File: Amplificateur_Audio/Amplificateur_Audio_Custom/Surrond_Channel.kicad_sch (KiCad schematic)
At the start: 80 parts, among them J401 SL+, J402 SL-, J403 SR+, J404 SR-, J405 Analog input Connector, U401 PCM5252RHBR, U402 TPA3244DDWR, U403 74LVC1G125, U404 74LVC1G125

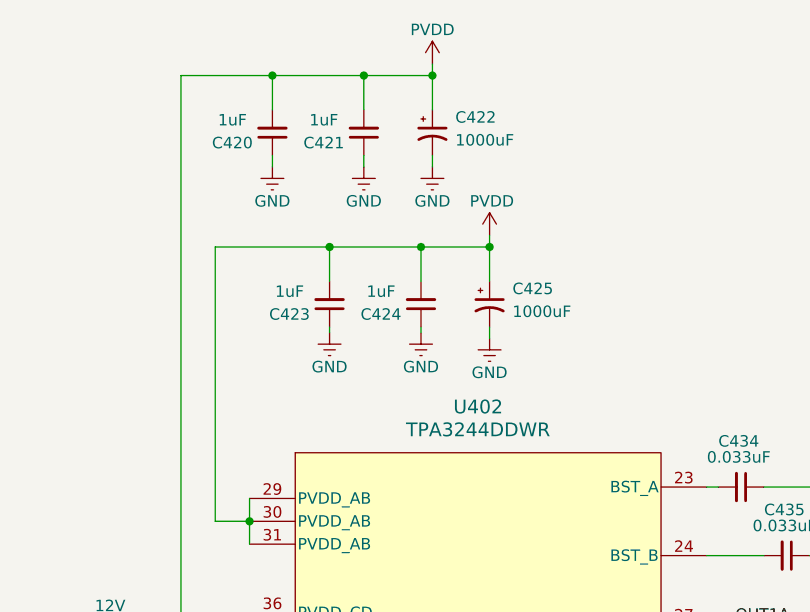
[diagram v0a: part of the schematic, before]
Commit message: Placement casi définitif prochaine étape vias de GND + stitching
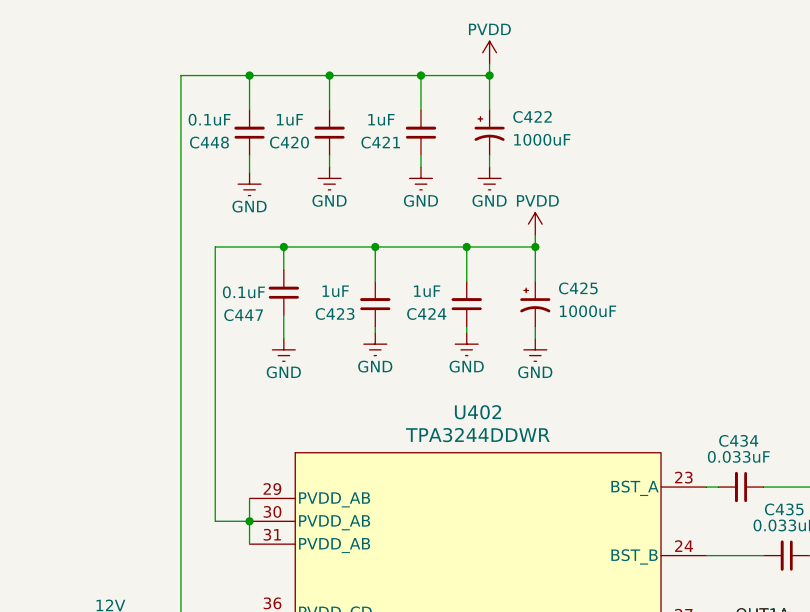
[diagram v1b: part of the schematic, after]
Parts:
- added C447, C448: 0.1uF, Capacitor_SMD:C_0603_1608Metric, symbol Device:C_Small
- C410, C411, C432, C433: footprint Capacitor_SMD:C_0402_1005Metric_Pad0.74x0.62mm_HandSolder -> Capacitor_SMD:C_0402_1005Metric
- C420, C421, C423, C424: footprint Capacitor_SMD:C_1206_3216Metric_Pad1.33x1.80mm_HandSolder -> Capacitor_SMD:C_1206_3216Metric
- C434, C435, C437, C439, C442, C443, C444, C445: footprint Capacitor_SMD:C_0603_1608Metric_Pad1.08x0.95mm_HandSolder -> Capacitor_SMD:C_0603_1608Metric
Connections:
- net GND: now also C447.1, C448.1
- net PVDD: now also C447.2, C448.2
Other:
- moved on the sheet: C420, C421, C422, C423, C424, C425

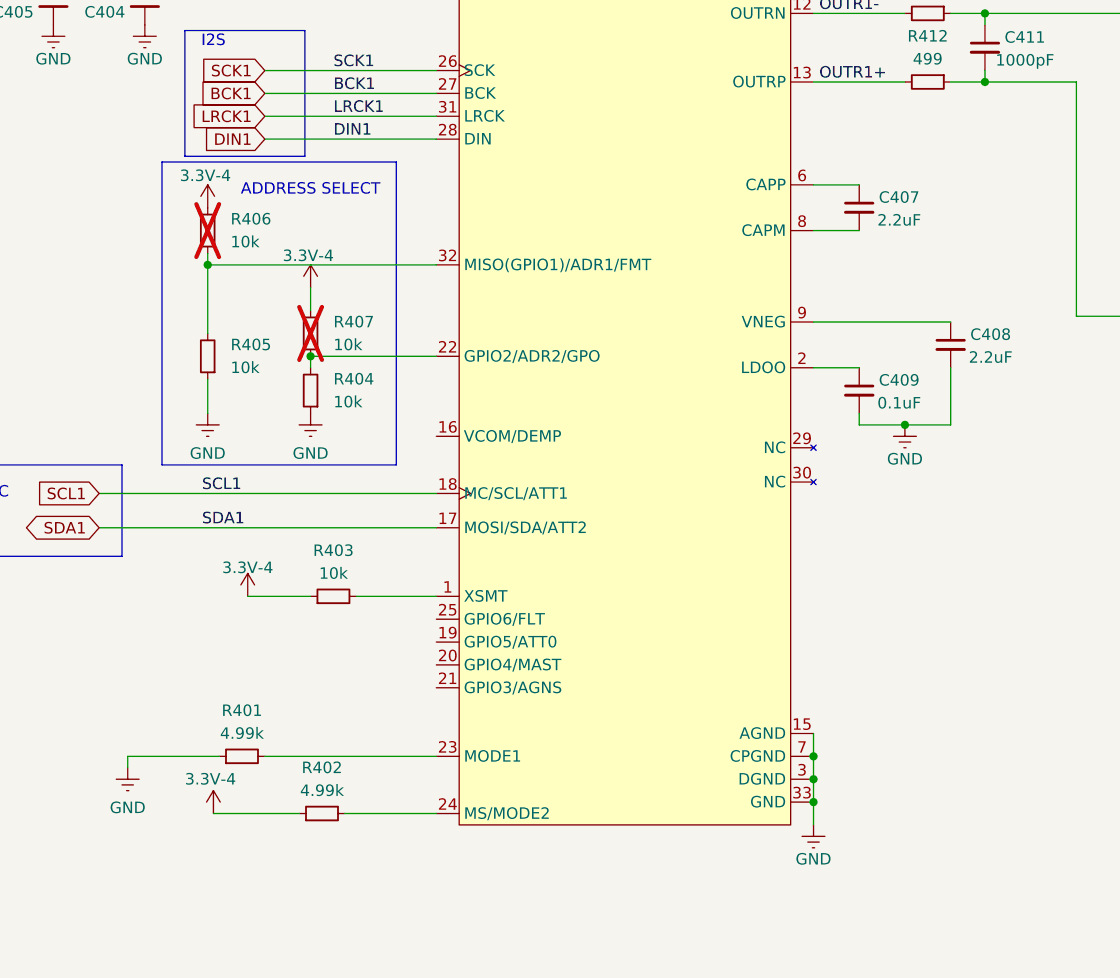
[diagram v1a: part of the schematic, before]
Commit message: Affinage du routage
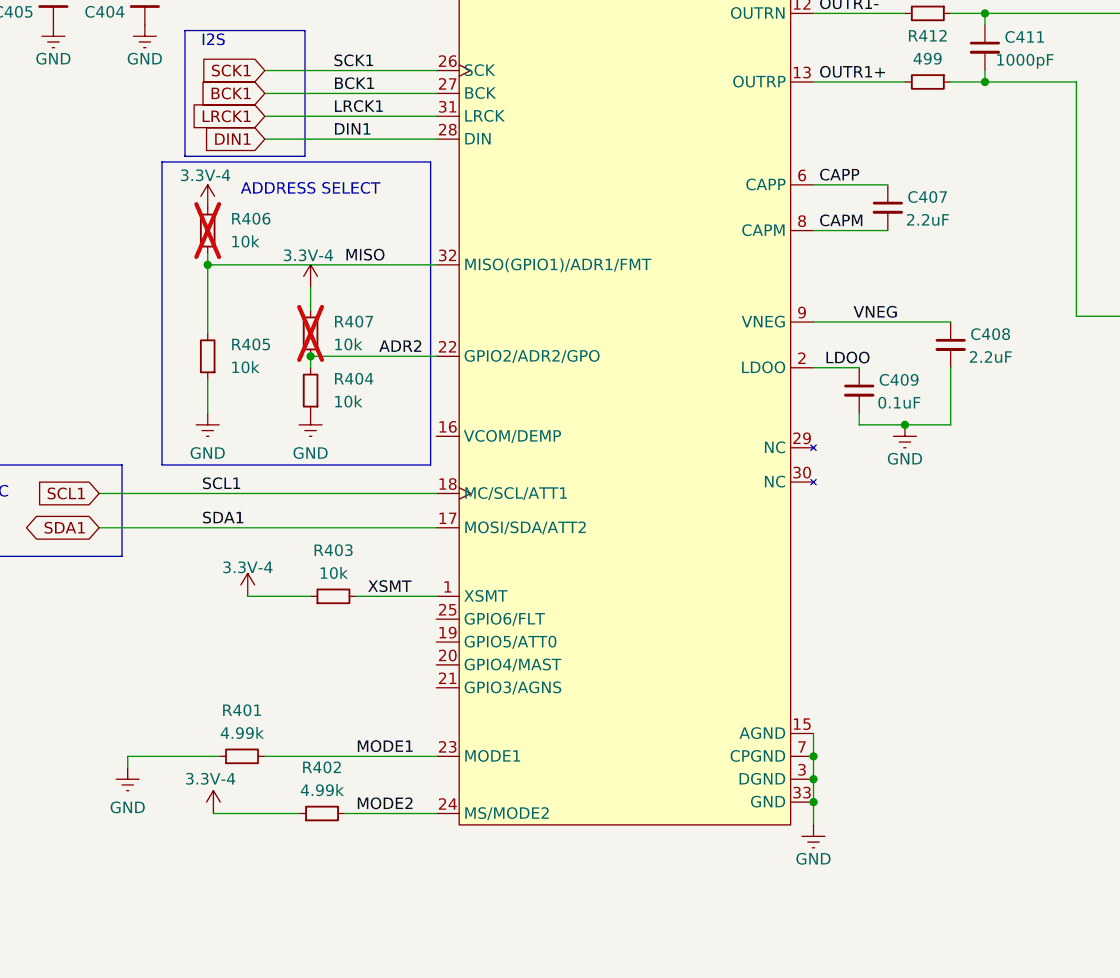
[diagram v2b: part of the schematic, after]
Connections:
- net LDOO: now reaches C409.1, U401.2 (LDOO)
- net ADR2: now reaches R404.2, R407.1, U401.22 (GPIO2/ADR2/GPO)
- net VNEG: now reaches C408.1, U401.9 (VNEG)
- net CAPP: now reaches C407.1, U401.6 (CAPP)
- net CAPM: now reaches C407.2, U401.8 (CAPM)
- net XSMT: now reaches R403.2, U401.1 (XSMT)
- net MISO: now reaches R405.2, R406.1, U401.32 (MISO(GPIO1)/ADR1/FMT)
- net MODE2: now reaches R402.2, U401.24 (MS/MODE2)
- net MODE1: now reaches R401.2, U401.23 (MODE1)
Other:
- moved on the sheet: C407
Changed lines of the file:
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@@
 	(rectangle
 		(start 44.45 78.105)
-		(end 70.485 111.76)
+		(end 74.295 111.76)
 		(stroke
 			(width 0)
@@
 	(wire
 		(pts
+			(xy 60.96 99.695) (xy 74.93 99.695)
+		)
+		(stroke
+			(width 0)
+			(type default)
+		)
+	)
+	(wire
+		(pts
 			(xy 370.205 97.155) (xy 370.205 94.615)
 		)
@@
 	(wire
 		(pts
-			(xy 74.93 99.695) (xy 60.96 99.695)
-		)
-		(stroke
-			(width 0)
-			(type default)
-		)
-	)
-	(wire
-		(pts
 			(xy 321.31 114.935) (xy 321.31 117.475)
 		)
@@
 	(wire
 		(pts
-			(xy 121.92 85.725) (xy 116.84 85.725)
+			(xy 125.095 85.725) (xy 116.84 85.725)
 		)
 		(stroke
@@
 	(wire
 		(pts
-			(xy 121.92 80.645) (xy 116.84 80.645)
+			(xy 125.095 80.645) (xy 116.84 80.645)
 		)
 		(stroke
@@
 		)
 	)
+	(label "VNEG"
+		(at 121.285 95.885 0)
+		(effects
+			(font
+				(size 1.27 1.27)
+			)
+			(justify left bottom)
+		)
+	)
 	(label "OSC-IOM"
 		(at 368.3 233.68 0)
@@
 		)
 	)
+	(label "ADR2"
+		(at 68.58 99.695 0)
+		(effects
+			(font
+				(size 1.27 1.27)
+			)
+			(justify left bottom)
+		)
+	)
 	(label "INPUTL1+"
 		(at 259.08 132.715 0)
@@
 		)
 	)
+	(label "LDOO"
+		(at 118.11 100.965 0)
+		(effects
+			(font
+				(size 1.27 1.27)
+			)
+			(justify left bottom)
+		)
+	)
 	(label "INC5"
 		(at 48.26 260.35 0)
@@
 		)
 	)
+	(label "CAPP"
+		(at 117.475 80.645 0)
+		(effects
+			(font
+				(size 1.27 1.27)
+			)
+			(justify left bottom)
+		)
+	)
+	(label "MISO"
+		(at 64.77 89.535 0)
+		(effects
+			(font
+				(size 1.27 1.27)
+			)
+			(justify left bottom)
+		)
+	)
 	(label "OUT1D"
 		(at 342.9 113.665 0)
@@
 		)
 	)
+	(label "MODE2"
+		(at 66.04 150.495 0)
+		(effects
+			(font
+				(size 1.27 1.27)
+			)
+			(justify left bottom)
+		)
+	)
 	(label "INB4"
 		(at 48.26 247.65 0)
@@
 		)
 	)
+	(label "MODE1"
+		(at 66.04 144.145 0)
+		(effects
+			(font
+				(size 1.27 1.27)
+			)
+			(justify left bottom)
+		)
+	)
 	(label "SurroundRight-"
 		(at 382.905 132.715 0)
@@
 		)
 	)
+	(label "CAPM"
+		(at 117.475 85.725 0)
+		(effects
+			(font
+				(size 1.27 1.27)
+			)
+			(justify left bottom)
+		)
+	)
+	(label "XSMT"
+		(at 67.31 126.365 0)
+		(effects
+			(font
+				(size 1.27 1.27)
+			)
+			(justify left bottom)
+		)
+	)
 	(label "Surrond Left-"
 		(at 381 88.265 0)
@@
 	(symbol
 		(lib_id "Device:C_Small")
-		(at 121.92 83.185 0)
+		(at 125.095 83.185 0)
 		(unit 1)
 		(exclude_from_sim no)
@@
 		(dnp no)
 		(property "Reference" "C407"
-			(at 126.365 82.042 0)
+			(at 129.54 82.042 0)
 			(effects
 				(font
@@
 		)
 		(property "Value" "2.2uF"
-			(at 126.365 84.582 0)
+			(at 129.54 84.582 0)
 			(effects
 				(font
@@
 		)
 		(property "Footprint" "Capacitor_SMD:C_0402_1005Metric"
-			(at 121.92 83.185 0)
+			(at 125.095 83.185 0)
 			(effects
 				(font
@@
 		)
 		(property "Datasheet" "~"
-			(at 121.92 83.185 0)
+			(at 125.095 83.185 0)
 			(effects
 				(font
@@
 		)
 		(property "Description" "C1005X5R1A225K050BC"
-			(at 121.92 83.185 0)
+			(at 125.095 83.185 0)
 			(effects
 				(font

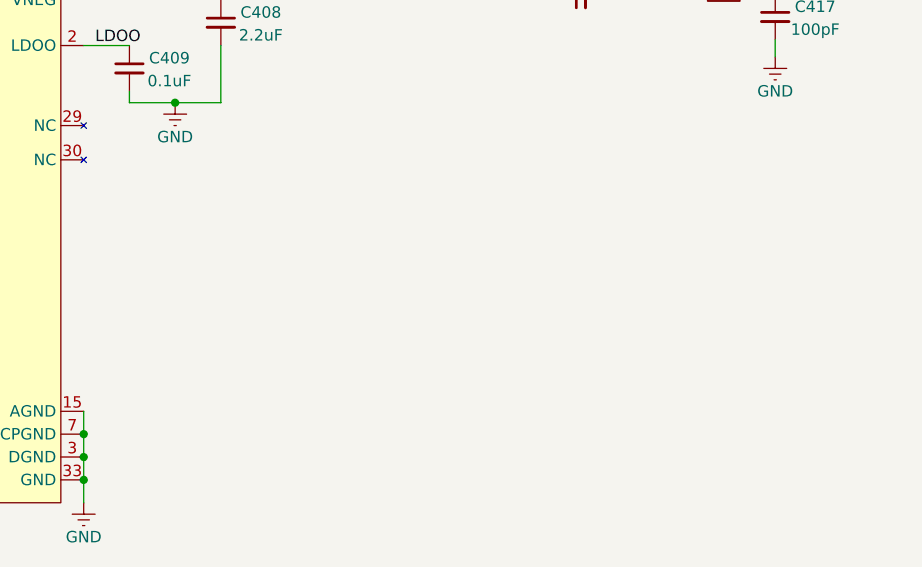
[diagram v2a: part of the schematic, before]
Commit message: Routage finale pour Surround Channel, publication d'une backup avant clonage grace au multichannel
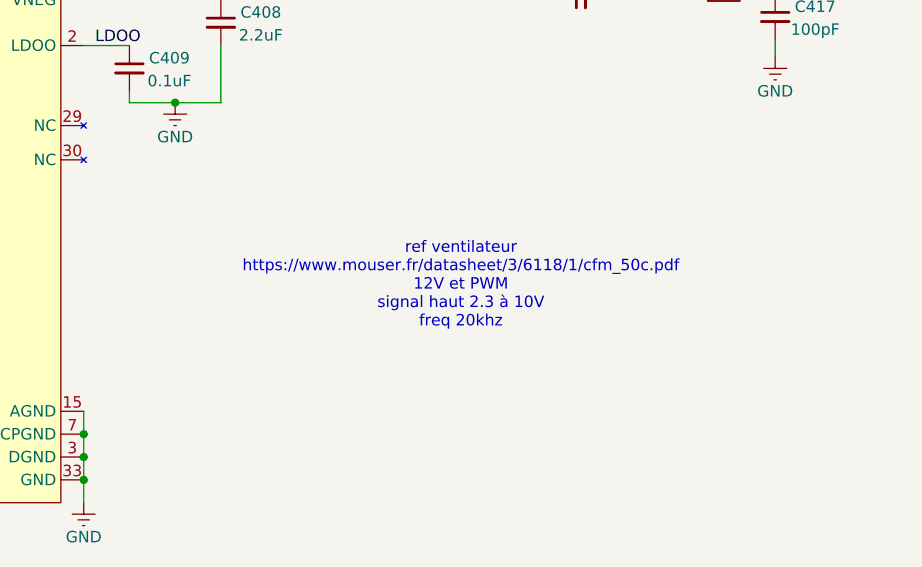
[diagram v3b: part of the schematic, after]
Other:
- note added: "ref ventilateur https://www.mouser.fr/datasheet/3/6118/1/cfm_50c.pdf 12V et PWM signal haut 2.3 à 10V freq 20khz"
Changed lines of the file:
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@@
 		)
 	)
+	(text "ref ventilateur \nhttps://www.mouser.fr/datasheet/3/6118/1/cfm_50c.pdf\n12V et PWM\nsignal haut 2.3 à 10V\nfreq 20khz\n"
+		(exclude_from_sim no)
+		(at 158.75 127.635 0)
+		(effects
+			(font
+				(size 1.27 1.27)
+			)
+		)
+	)
 	(text "Surround"
 		(exclude_from_sim no)
@@
 			)
 		)
+	)
+	(rule_area
+		(polyline
+			(pts
+				(xy 218.44 15.24) (xy 218.44 215.265) (xy 320.675 215.265) (xy 327.025 208.915) (xy 327.025 179.705)
+				(xy 330.835 175.895) (xy 391.16 175.895) (xy 407.035 160.02) (xy 407.035 52.705) (xy 369.57 15.24)
+			)
+			(stroke
+				(width 0)
+				(type dash)
+			)
+			(fill
+				(type none)
+			)
+		)
+	)
+	(rule_area
+		(polyline
+			(pts
+				(xy 216.535 35.56) (xy 216.535 140.335) (xy 196.85 160.02) (xy 19.685 160.02) (xy 12.7 153.035)
+				(xy 12.7 31.115) (xy 29.845 13.97) (xy 194.945 13.97)
+			)
+			(stroke
+				(width 0)
+				(type dash)
+			)
+			(fill
+				(type none)
+			)
+		)
+	)
+	(netclass_flag ""
+		(length 2.54)
+		(shape round)
+		(at 12.7 31.115 0)
+		(fields_autoplaced yes)
+		(effects
+			(font
+				(size 1.27 1.27)
+			)
+			(justify left bottom)
+		)
+		(property "Netclass" ""
+			(at -231.14 27.305 0)
+			(effects
+				(font
+					(size 1.27 1.27)
+				)
+			)
+		)
+		(property "Component Class" "Préampli"
+			(at 13.3985 28.575 0)
+			(effects
+				(font
+					(size 1.27 1.27)
+					(italic yes)
+				)
+				(justify left)
+			)
+		)
+	)
+	(netclass_flag ""
+		(length 2.54)
+		(shape round)
+		(at 218.44 15.24 0)
+		(fields_autoplaced yes)
+		(effects
+			(font
+				(size 1.27 1.27)
+			)
+			(justify left bottom)
+		)
+		(property "Netclass" ""
+			(at -116.84 10.16 0)
+			(effects
+				(font
+					(size 1.27 1.27)
+				)
+			)
+		)
+		(property "Component Class" "Ampli"
+			(at 219.1385 12.7 0)
+			(effects
+				(font
+					(size 1.27 1.27)
+					(italic yes)
+				)
+				(justify left)
+			)
+		)
